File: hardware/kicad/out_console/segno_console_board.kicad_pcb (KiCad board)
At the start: 2 copper layers, 99.5 x 99.5 mm, 62 parts, among them J1 RaspberryPi_Pico_SMD_HandSold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, J10 JST_XH_B2B-XH-A_1x02_P2.50mm_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, J11 JST_XH_B2B-XH-A_1x02_P2.50mm_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, J12 JST_XH_B2B-XH-A_1x02_P2.50mm_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, J13 JST_XH_B2B-XH-A_1x02_P2.50mm_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, J14 JST_XH_B2B-XH-A_1x02_P2.50mm_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, J15 JST_XH_B2B-XH-A_1x02_P2.50mm_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, J16 JST_XH_B2B-XH-A_1x02_P2.50mm_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, J17 JST_XH_B2B-XH-A_1x02_P2.50mm_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, J18 JST_XH_B2B-XH-A_1x02_P2.50mm_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, J19 JST_XH_B2B-XH-A_1x02_P2.50mm_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, J2 IDC-Header_2x20_P2.54mm_Verti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, J20 JST_XH_B3B-XH-A_1x03_P2.50mm_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, J21 JST_XH_B3B-XH-A_1x03_P2.50mm_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, J22 PinHeader_2x04_P2.54mm_Vertic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, J3 JST_XH_B4B-XH-A_1x04_P2.50mm_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, J4 JST_XH_B3B-XH-A_1x03_P2.50mm_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, J5 JST_XH_B2B-XH-A_1x02_P2.50mm_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, J6 JST_XH_B4B-XH-A_1x04_P2.50mm_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, J7 JST_XH_B3B-XH-A_1x03_P2.50mm_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, J8 JST_XH_B2B-XH-A_1x02_P2.50mm_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, J9 JST_XH_B2B-XH-A_1x02_P2.50mm_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, U1 DIP-14_W7.62mm, U2 DIP-6_W7.62mm

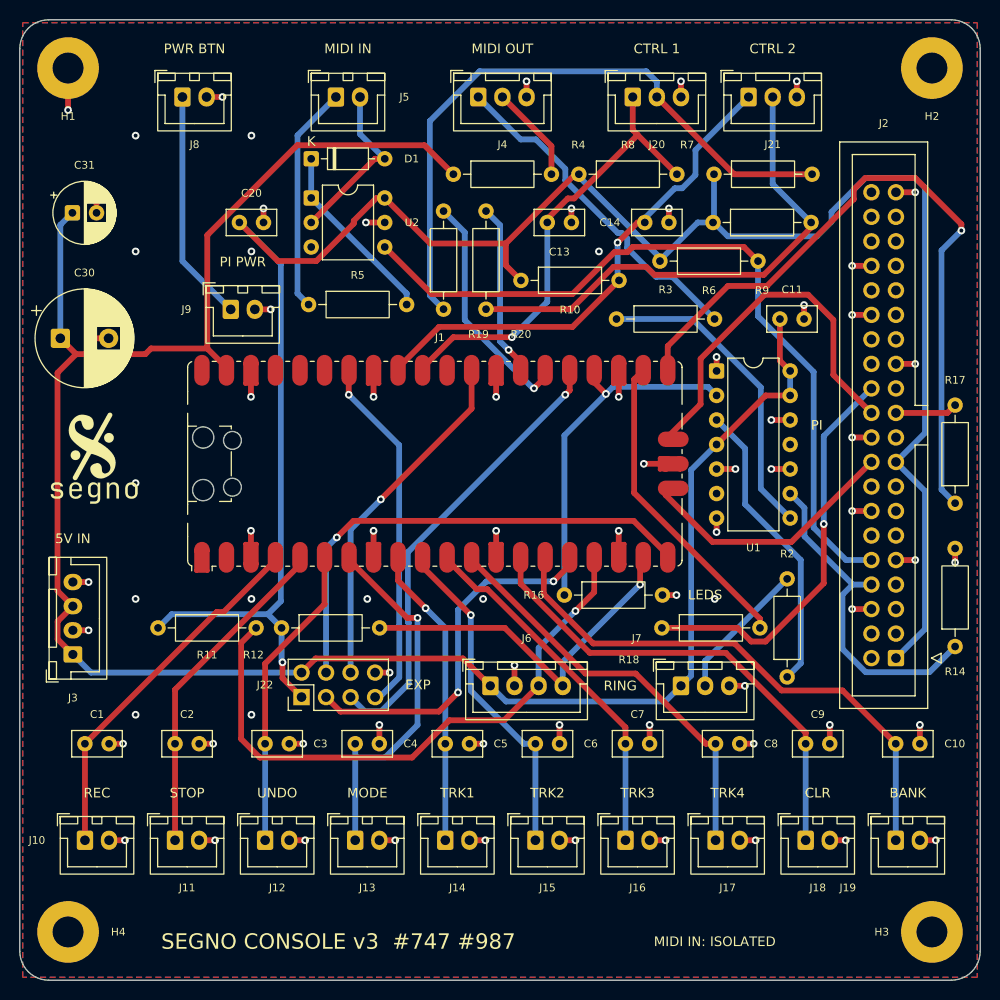
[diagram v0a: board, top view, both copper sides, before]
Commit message: feat(hardware): console board v3 — read the PD trigger's contract over I2C
The console cannot tell whether the STUSB4500 negotiated 20 V / 5 A or a
65 W brick's 20 V / 3.25 A: both boot, and the second browns out only when
the LEDs go white under two lit screens. The chip is I2C-readable (RDO at
0x91-0x94 with capaMismatch, voltage at 0x21), so v3 gives it a header.

J23 PD: JST-XH 3-way — GND, SDA, SCL on GP0/GP1 (I2C0, the pins v2 left
spare), under the module's left end beside 5V IN; R11/R12 rise 3 mm to make
the row. Three wires on purpose: the breakout's VDD and pull-ups come off
VBUS on its own board, and this board's 3V3 is downstream of the contract
being measured. A gate now asserts the pair is one I2C instance's SDA/SCL,
and no GPIO on the module is spare any more (the UART self-test that leaned
on GP1 being free swaps pins instead).

Routed clean: 0 DRC violations, 0 unconnected, ratsnest 1725 mm of 1770.
Silk keep-outs and back art regenerated for the new pad set.

Firmware for the read and its pedal-link report is not written yet; the
wiring doc, the soldering guide's v3 table and the firmware README say so.
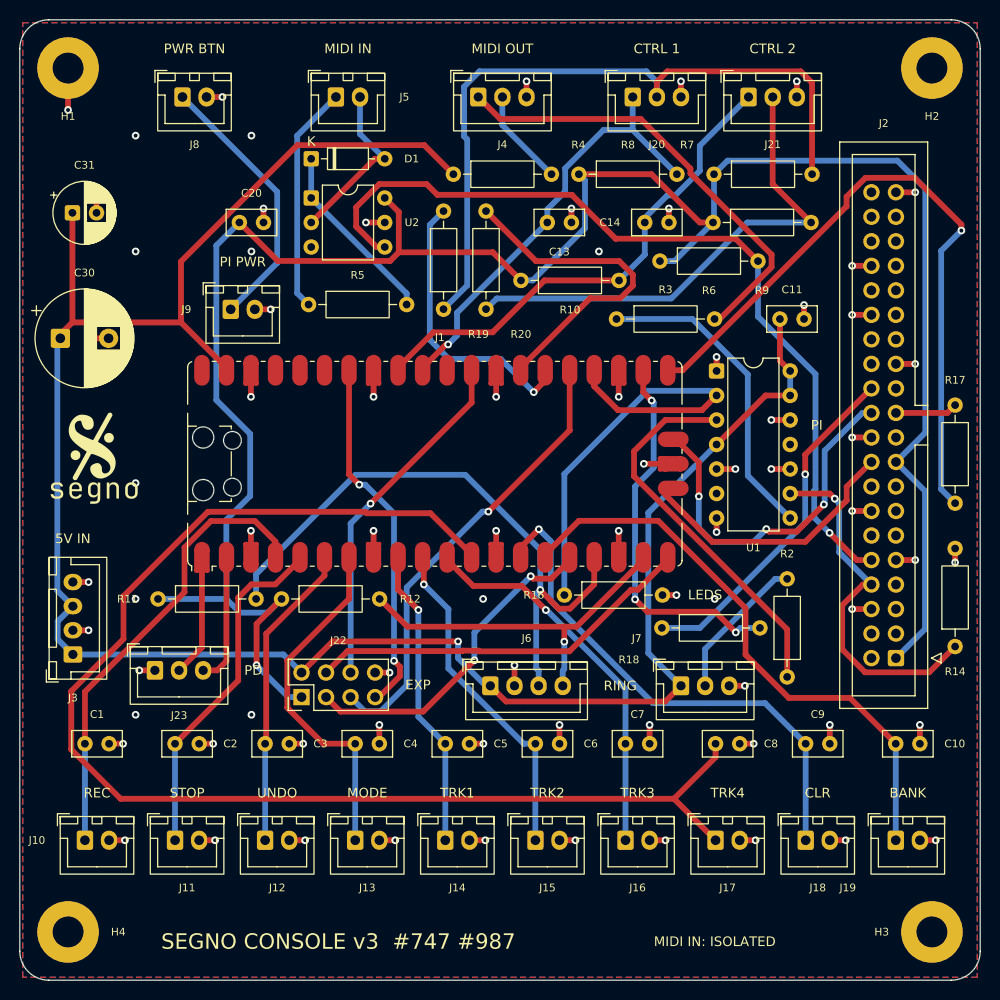
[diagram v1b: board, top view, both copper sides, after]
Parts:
- added J23: JST_XH_B3B-XH-A_1x03_P2.50mm_Vertical, JST_XH_B3B-XH-A_1x03_P2.50mm_Vertical, F.Cu at (114.0, 127.4)
- moved R11 3.00 mm to (114.3, 120.0)
- moved R12 3.00 mm to (127.1, 120.0)
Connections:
- J1 pad 1: (no net) -> PD_SDA
- J1 pad 2: (no net) -> PD_SCL
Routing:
- net SW_TRACK4: track 43.4 -> 138.1 mm
- net CTRL2_RING: track 18.0 -> 34.5 mm, vias 1 -> 0
- net PD_SCL: track 0.00 -> 13.6 mm
- net PD_SDA: track 0.00 -> 12.7 mm
- net N$1: track 35.3 -> 46.9 mm
- net +3V3: track 217.1 -> 228.1 mm
- net EXP_GP15: track 51.2 -> 40.6 mm, vias 1 -> 0
- net IND_DATA: track 37.7 -> 48.1 mm, vias 1 -> 0
- net SW_RECPLAY: track 37.9 -> 47.7 mm
- net IND_DATA_BUF: track 30.8 -> 39.8 mm
- net MIDI_RX: track 80.7 -> 88.6 mm, vias 0 -> 1
- net J20_REF: track 67.2 -> 74.9 mm
- net LINK_RX: track 32.5 -> 39.5 mm, vias 0 -> 3
- net LINK_RX_PI: track 42.1 -> 36.1 mm
- net CTRL1_RING: track 24.7 -> 29.7 mm
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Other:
- board text added: "PD"

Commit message: fix(hardware): v3 — EXP back where v2 had it, PD in the RING row
Bench feedback on the v3 layout: the expansion header was liked where v2 put
it, and the PD header sat 1.6 mm above the row it belongs to.

J22 returns to the column beside U2. R19/R20, which had taken that column
to stay under the jacks, move to the row R13 and R15 left empty under the
module; their nets are DC sense lines through 4.7 k, so the 50-60 mm run
does not matter, and the hop gate exempts them by name with that reason
(SLOW_SENSE_NETS). J23 drops onto the RING/LEDS row.

The silk keep-out list now covers every pad that opens the back mask, not
only plated ones: the Pico's three NPTH anchors were missed and the big
segno landed on them (silk_over_copper). Routed clean: 0 violations,
0 unconnected, ratsnest 1707 mm of 1770. Gerbers regenerated.
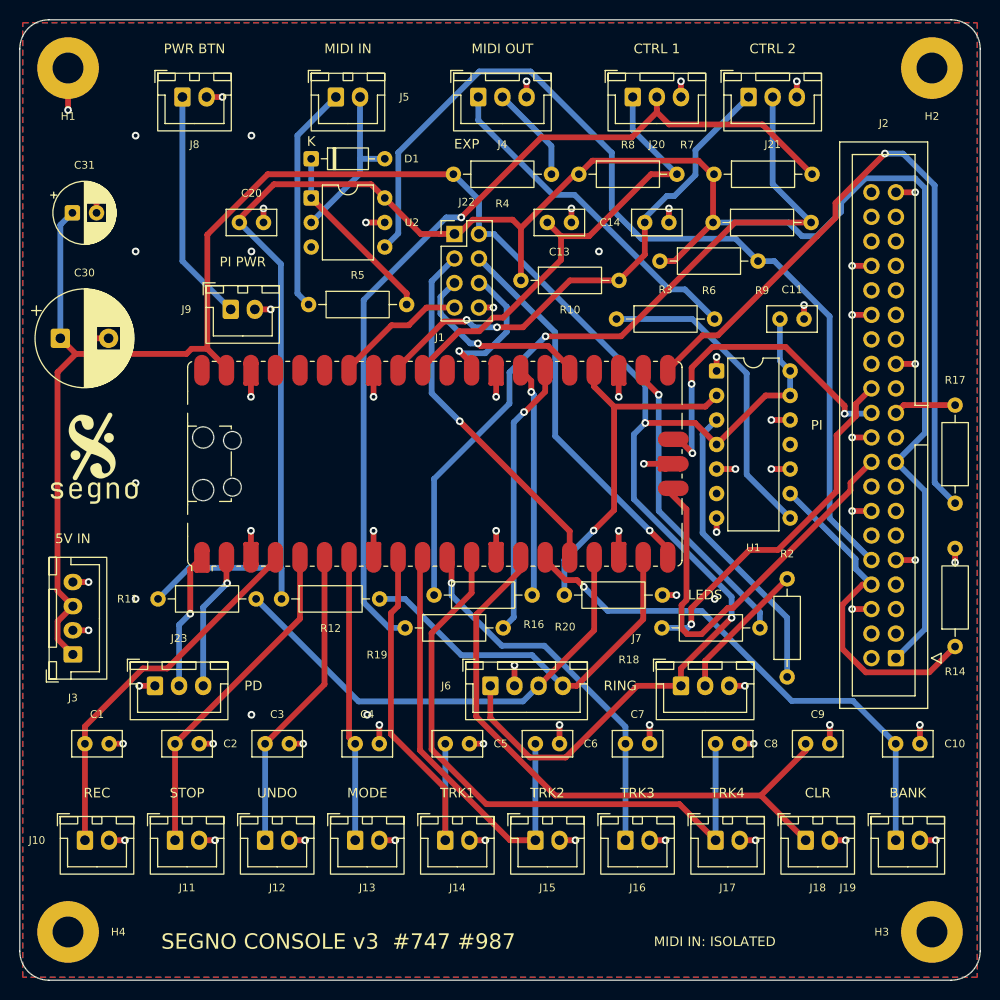
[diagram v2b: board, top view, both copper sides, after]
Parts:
- moved J22 50.5 mm to (145.0, 82.2), turned to 0 degrees
- moved R19 33.3 mm to (139.9, 123.0), turned to 0 degrees
- moved R20 30.1 mm to (142.9, 119.6), turned to 0 degrees
- moved J23 1.60 mm to (114.0, 129.0)
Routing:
- net SW_TRACK4: track 138.1 -> 64.9 mm
- net EXP_GP19: track 47.5 -> 19.8 mm
- net J21_REF: track 52.0 -> 78.6 mm, vias 0 -> 1
- net EXP_GP28: track 37.7 -> 13.8 mm, vias 2 -> 0
- net EXP_GP22: track 36.5 -> 15.0 mm
- net J20_REF: track 74.9 -> 95.5 mm, vias 0 -> 1
- net +3V3: track 228.1 -> 208.5 mm, vias 1 -> 0
- net SWCLK: track 28.3 -> 43.4 mm
- net LINK_TO_RING: track 64.1 -> 50.0 mm, vias 1 -> 0
- net N$1: track 46.9 -> 35.4 mm
- net SW_TRACK2: track 34.9 -> 45.9 mm, vias 1 -> 0
- net SW_CLEAR: track 54.2 -> 65.1 mm, vias 1 -> 0
- net MIDI_RX: track 88.6 -> 99.5 mm, vias 1 -> 0
- net IND_DATA: track 48.1 -> 37.4 mm, vias 0 -> 1
- net SW_TRACK1: track 31.3 -> 41.9 mm, vias 1 -> 0
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
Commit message: fix(hardware): back-silk art — the segno stays whole, the year keeps off the name
The composer placed a fixed 32 mm segno at the least-obstructed spot and let
the pad carve punch through it; on v3 that left the mark with pins cut out
of it. Now it searches sizes from 32 mm down and positions on a 0.5 mm
grid, and keeps the largest at which the glyph's own outline touches no
back-mask opening, nearest the board's middle. 28 mm fits whole. The staff
and the waveform are still carved: lines are meant to be interrupted, a mark
is not.

The year used to land 1.5 mm under the wordmark, through its descenders,
because the text search never excluded the wordmark's own ground. It now
goes on the wordmark's baseline a word-space after it, measured from the
set width rather than a per-character estimate (which was 12 mm short).

Routed clean: 0 violations, 0 unconnected. Gerbers regenerated.
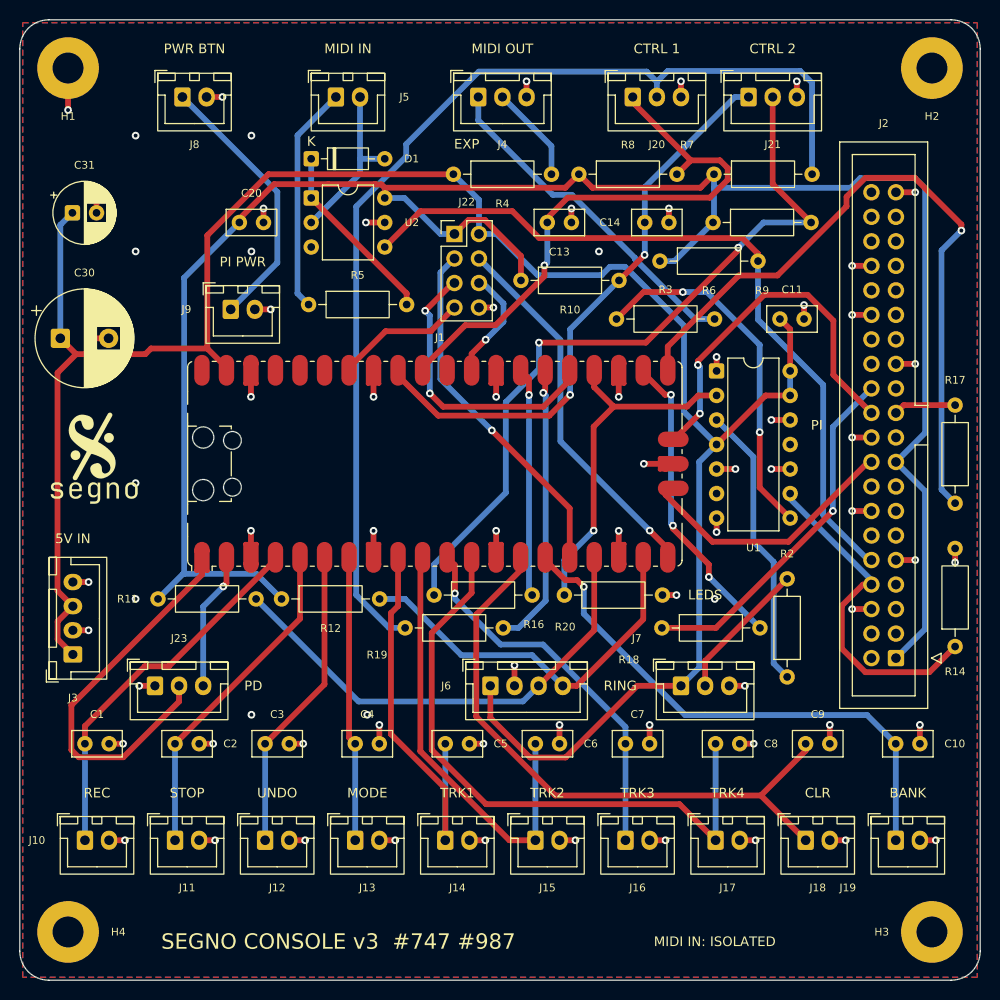
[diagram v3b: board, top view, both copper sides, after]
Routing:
- net PD_SDA: track 14.3 -> 41.0 mm, vias 1 -> 0
- net MIDI_RX: track 99.5 -> 78.8 mm
- net J20_REF: track 95.5 -> 112.9 mm, vias 1 -> 0
- net SWCLK: track 43.4 -> 27.4 mm
- net CTRL1_TIP: track 48.2 -> 59.7 mm, vias 0 -> 1
- net EXP_GP19: track 19.8 -> 30.2 mm, vias 1 -> 2
- net CTRL2_TIP: track 52.6 -> 60.3 mm
- net +3V3: track 208.5 -> 215.4 mm
- net MIDI_OUT_BUF: track 32.7 -> 37.5 mm, vias 0 -> 2
- net SWDIO: track 35.2 -> 39.4 mm, vias 3 -> 2
- net PWR_BTN: track 24.1 -> 28.1 mm
- net +5V: track 229.7 -> 225.8 mm, vias 2 -> 0
- net EXP_GP22: track 15.0 -> 11.7 mm
- net SW_BANK: track 54.5 -> 56.1 mm
- net IND_DATA_BUF: track 30.9 -> 29.6 mm
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
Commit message: feat(hardware): console board v3 — switched CTRL jacks report presence
The CTRL jacks become Neutrik NJ6FD-V: D-series like the jack they
replace, same Ø24 punch and M3 pair, with switching contacts. Each jack's
tip-normal contact goes to the board as a fourth lead (J20/J21 are 4-way
now) and through 4.7 k (R21/R22) to GP19/GP22. The contact ties to the
tip — 3V3 through 10 k — while the jack is empty and opens once a plug is
in, so with the RP2350's pull-down the pin is high only for an empty jack.
Presence becomes a wire: an empty jack no longer reads as a pedal at full
toe, and a plug on its way in is ignored until it is seated. Firmware 1.2
reads it; on a v2 board the same pins float on J22's pads and read
"plugged", so one firmware serves both.

GP19/GP22 leave J22, which is 2x3 (GP12, GP15, GP28). The CTRL headers
slide 2.6 mm left to keep their clearances at 4-way width; R11/R12 join
R16/R20 on the band under the module so the row below is R21/R22's.

Ratsnest 1915 mm: the four sense nets run 50-60 mm to parts under the
module by decision (DC through 4.7 k, exempt from the hop gate), so the
budget follows the measurement to 2050 with that reason next to it. Routed
clean: 0 violations, 0 unconnected. Gerbers, BOM and art regenerated.

Docs: shopping list (NJ6FD-V x2, four leads), soldering guide's v3 table,
wiring, firmware README pin table.
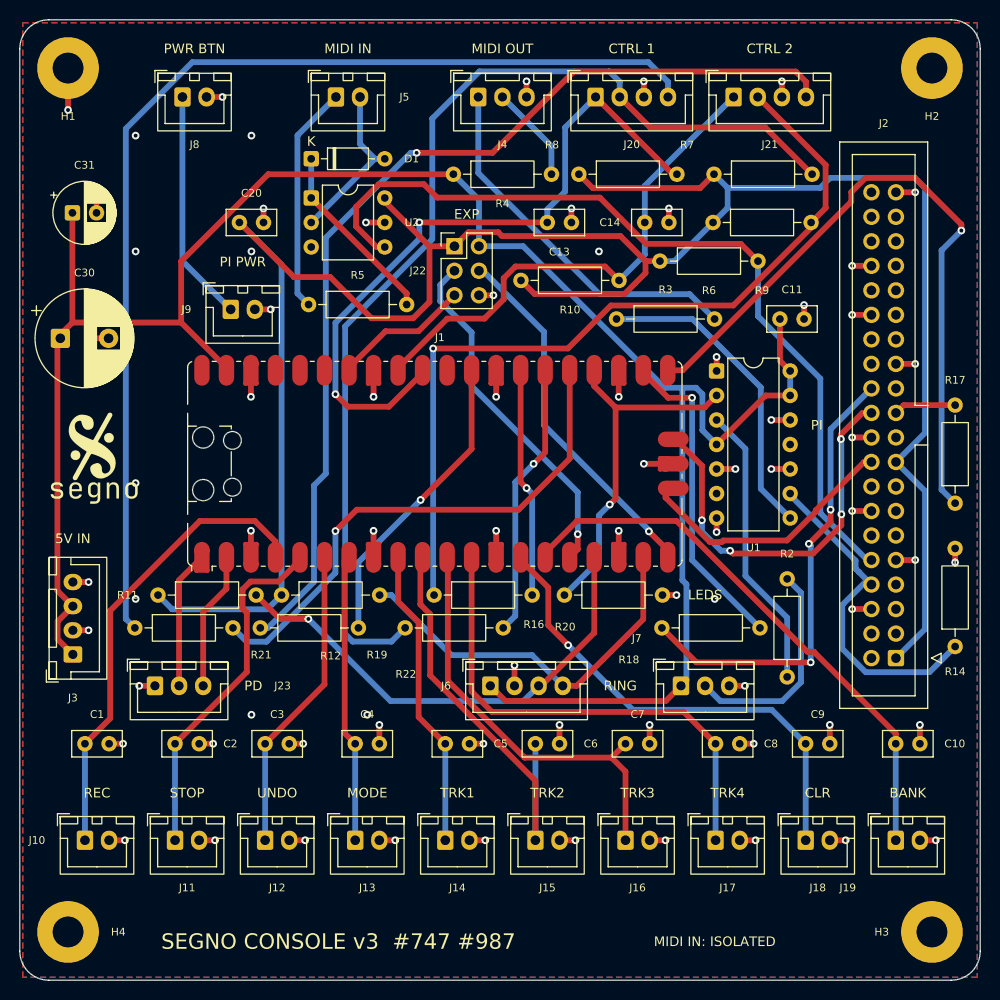
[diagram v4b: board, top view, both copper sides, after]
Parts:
- added R21: R_Axial_DIN0207_L6.3mm_D2.5mm_P10.16mm_Horizontal, R_Axial_DIN0207_L6.3mm_D2.5mm_P10.16mm_Horizontal, F.Cu at (111.9, 123.0)
- added R22: R_Axial_DIN0207_L6.3mm_D2.5mm_P10.16mm_Horizontal, R_Axial_DIN0207_L6.3mm_D2.5mm_P10.16mm_Horizontal, F.Cu at (124.9, 123.0)
- J20, J21: value JST_XH_B3B-XH-A_1x03_P2.50mm_Vertical -> JST_XH_B4B-XH-A_1x04_P2.50mm_Vertical; footprint JST_XH_B3B-XH-A_1x03_P2.50mm_Vertical -> JST_XH_B4B-XH-A_1x04_P2.50mm_Vertical
- J22: value PinHeader_2x04_P2.54mm_Vertical -> PinHeader_2x03_P2.54mm_Vertical; footprint PinHeader_2x04_P2.54mm_Vertical -> PinHeader_2x03_P2.54mm_Vertical
- moved J20 3.85 mm to (159.7, 68.0)
- moved J21 1.55 mm to (173.9, 68.0)
- moved J22 1.27 mm to (145.0, 83.5)
- moved R11 0.40 mm to (114.3, 119.6)
- moved R12 0.40 mm to (127.1, 119.6)
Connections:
- J1 pad 25: EXP_GP19 -> CTRL1_PRESENT
- J1 pad 29: EXP_GP22 -> CTRL2_PRESENT
- J22 pad 5: EXP_GP19 -> EXP_GP28
- J22 pad 6: EXP_GP22 -> GND
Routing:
- net J20_TN: track 0.00 -> 113.5 mm
- net J21_TN: track 0.00 -> 102.6 mm, vias 0 -> 1
- net CTRL1_PRESENT: track 0.00 -> 55.0 mm, vias 0 -> 1
- net CTRL2_PRESENT: track 0.00 -> 31.5 mm, vias 0 -> 1
- net EXP_GP19: track 30.2 -> 0.00 mm, vias 2 -> 0
- net PD_SDA: track 41.0 -> 14.3 mm
- net +3V3: track 215.4 -> 235.3 mm
- net SW_CLEAR: track 65.1 -> 50.0 mm, vias 0 -> 1
- net SW_TRACK4: track 64.9 -> 51.4 mm
- net CTRL1_TIP: track 59.7 -> 72.8 mm, vias 1 -> 2
- net EXP_GP22: track 11.7 -> 0.00 mm, vias 1 -> 0
- net LINK_RX_PI: track 37.1 -> 48.0 mm, vias 1 -> 3
- net SW_TRACK1: track 41.9 -> 31.3 mm
- net SW_RECPLAY: track 38.9 -> 48.4 mm
- net MIDI_RX: track 78.8 -> 87.9 mm
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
